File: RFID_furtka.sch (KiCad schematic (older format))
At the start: 1 part

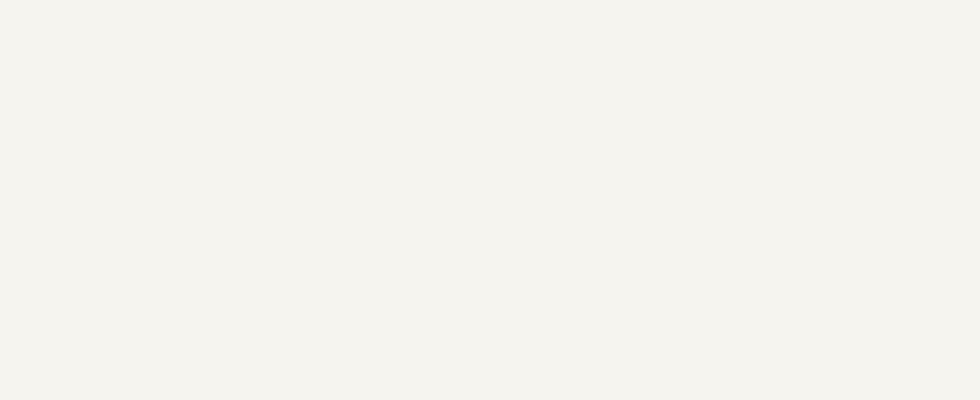
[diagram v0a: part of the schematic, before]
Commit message: Add LDO, Relay, ESP and MRFCC522
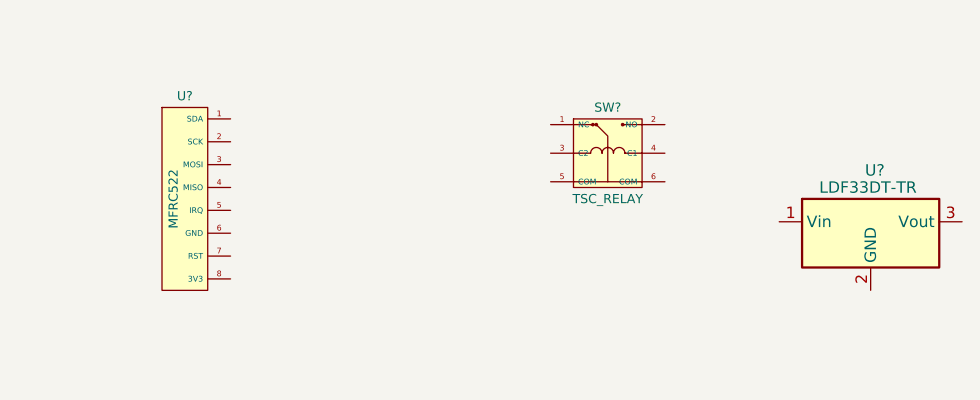
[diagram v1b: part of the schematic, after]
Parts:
- added SW?: TSC_RELAY, MyRelays:TSC-1XXX, symbol TSC_RELAY
- added U?: MFRC522, DevKits:MRFCC522, symbol MFRC522
- added U?: LDF33DT-TR, MyLDOs:DPAK, symbol LDF33DT-TR

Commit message: All components
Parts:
- added C? (x4): 10uF/16V, MyRLC:C_1611, symbol CP_Small
- added C? (x3): 100nF/50V, Capacitors_SMD:C_0805_HandSoldering, symbol C_Small
- added D?: 1n4148, Diodes_THT:D_DO-35_SOD27_P10.16mm_Horizontal, symbol D
- added D?: SS34, MyDiodesSMD:DO-214AB, symbol D
- added F?: 2A, Resistors_SMD:R_0805_HandSoldering, symbol Fuse
- added J?: CONN_01X03, MyConnectors:KF141R-2.54-3P, symbol CONN_01X03
- added Q?: SI2300DS, TO_SOT_Packages_SMD:SOT-23, symbol Q_NMOS_GSD
- added R?: 330K, Resistors_SMD:R_0805_HandSoldering, symbol R_Small
- added R?: 22R, Resistors_SMD:R_0603_HandSoldering, symbol R_Small
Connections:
- net relay: now reaches SW?.2 (NO)
- net relay: now also J?.1 (P1)
- net +12V: now reaches SW?.3 (C2)
- net +12V: now also U?.1 (Vin), C?.1, C?.1, D?.1 (K), D?.1 (K)
- net at SW?.4 (C1): now also D?.2 (A), Q?.3 (D)
- net GND: now reaches SW?.5 (COM)
- net GND: now also SW?.6 (COM), U?.2 (GND), C?.2, C?.2, C?.2, C?.2, J?.3 (P3), Q?.2 (S), R?.2
- net +3V3: now reaches U?.3 (Vout)
- net +3V3: now also C?.1, C?.1
- new net: D?.2 (A), F?.1
- new net: F?.2, J?.2 (P2)
- new net: Q?.1 (G), R?.1, R?.1
- new net open/close: R?.2
- no-connect marks 0 -> 1
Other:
- moved on the sheet: SW?, U?

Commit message: First PCB
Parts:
- removed C? (x2): 10uF/16V, MyRLC:C_1611, symbol CP_Small
- removed C?: 100nF/50V, Capacitors_SMD:C_0805_HandSoldering, symbol C_Small
- added C3: 10uF/16V, MyRLC:C_1611, symbol CP_Small
- added C5, C7, C8, C9: 100nF/50V, Capacitors_SMD:C_0805_HandSoldering, symbol C_Small
- gave numbers to parts that had none: 15
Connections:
- net +3V3: now also U2.8 (3V3), U3.11 (3V3), U3.21 (3V3), U3.30 (3v3), C3.1, C5.1, C7.1, C8.1, C9.1
- net GND: now also U2.6 (GND), U3.10 (GND), U3.14 (GND), U3.22 (GND), U3.29 (GND), C3.2, C5.2, C7.2, C8.2, C9.2
- net open/close: now also U3.17 (GPIO5_D1)
- net RST: now reaches U3.19 (FLASH_GPIO0_D3)
- net RST: now also U2.7 (RST)
- net SCK: now reaches U3.23 (HSCLK_GPIO14_D5)
- net SCK: now also U2.2 (SCK)
- net MISO: now reaches U3.24 (HMISO_GPIO12_D6)
- net MISO: now also U2.4 (MISO)
- net MOSI: now reaches U3.25 (HMOSI_RXD2_GPIO13_D7)
- net MOSI: now also U2.3 (MOSI)
- net SDA: now reaches U3.26 (HCS_TXD2_GPIO15_D8)
- net SDA: now also U2.1 (SDA)
- no-connect marks 1 -> 17
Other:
- note added: "LDO (12 V -> 3.3 V)"
- note added: "RFID + MCU"
- note added: "Relay"
- moved on the sheet: C1, C2, C4, C6, D1, D2, F1, J1, Q1, R1, R2, SW1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

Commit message: Fix few 3D bugs
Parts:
- D1: footprint MyDiodesSMD:DO-214AB -> Diodes_SMD:D_SMA_Handsoldering
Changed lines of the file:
@@
 F 0 "D1" H 2325 1600 50  0000 C CNN
 F 1 "SS34" H 2325 1400 50  0000 C CNN
-F 2 "MyDiodesSMD:DO-214AB" H 2325 1500 50  0001 C CNN
+F 2 "Diodes_SMD:D_SMA_Handsoldering" H 2325 1500 50  0001 C CNN
 F 3 "http://lispol.com/produkt/dioda-schottky-3a40v-sma---ss34" H 2325 1500 50  0001 C CNN
 	1    2325 1500

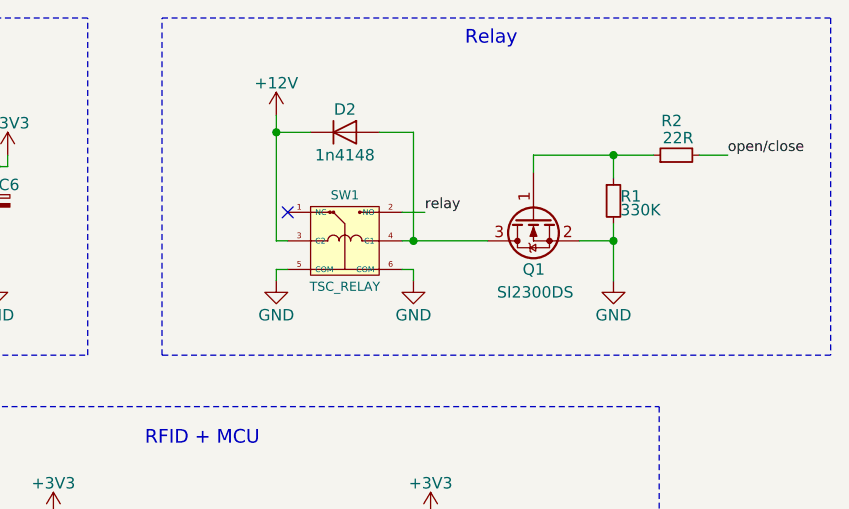
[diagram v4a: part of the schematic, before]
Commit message: Add comments about relay
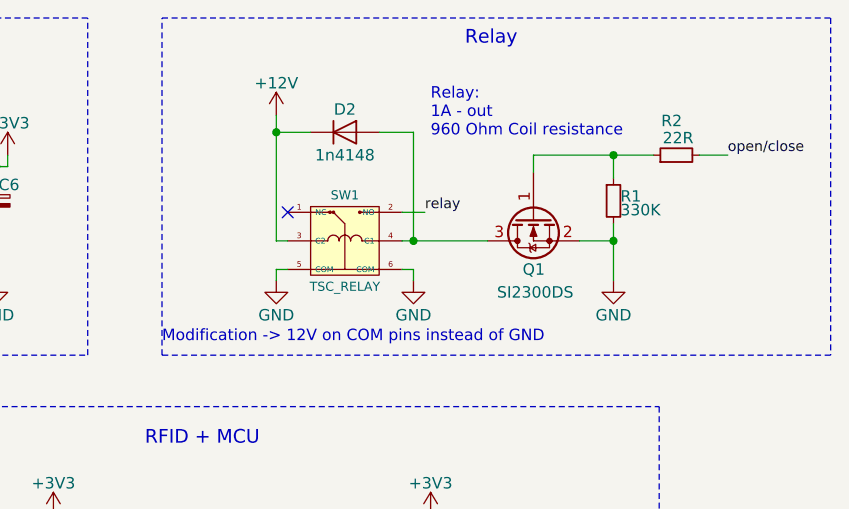
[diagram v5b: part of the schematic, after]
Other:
- note added: "Modification -> 12V on COM pins instead of GND"
- note added: "Relay:\n1A - out\n960 Ohm Coil resistance"
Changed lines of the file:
@@
 Wire Wire Line
 	6400 3275 6225 3275
+Text Notes 6375 1375 0    50   ~ 0
+Relay:\n1A - out\n960 Ohm Coil resistance
+Text Notes 5200 2275 0    50   ~ 0
+Modification -> 12V on COM pins instead of GND
 $EndSCHEMATC
